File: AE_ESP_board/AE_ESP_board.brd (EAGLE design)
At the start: 72 x 49 mm, 26 parts, among them CN1 SW_UART_IF, CN2 HW_UART_IF, CN3 POWER_IF, Q1 2N7000, Q2 2N7000, SW1 10-XX, U1 AE-ESP-WROOM-02, U2 M78AR033-0.5

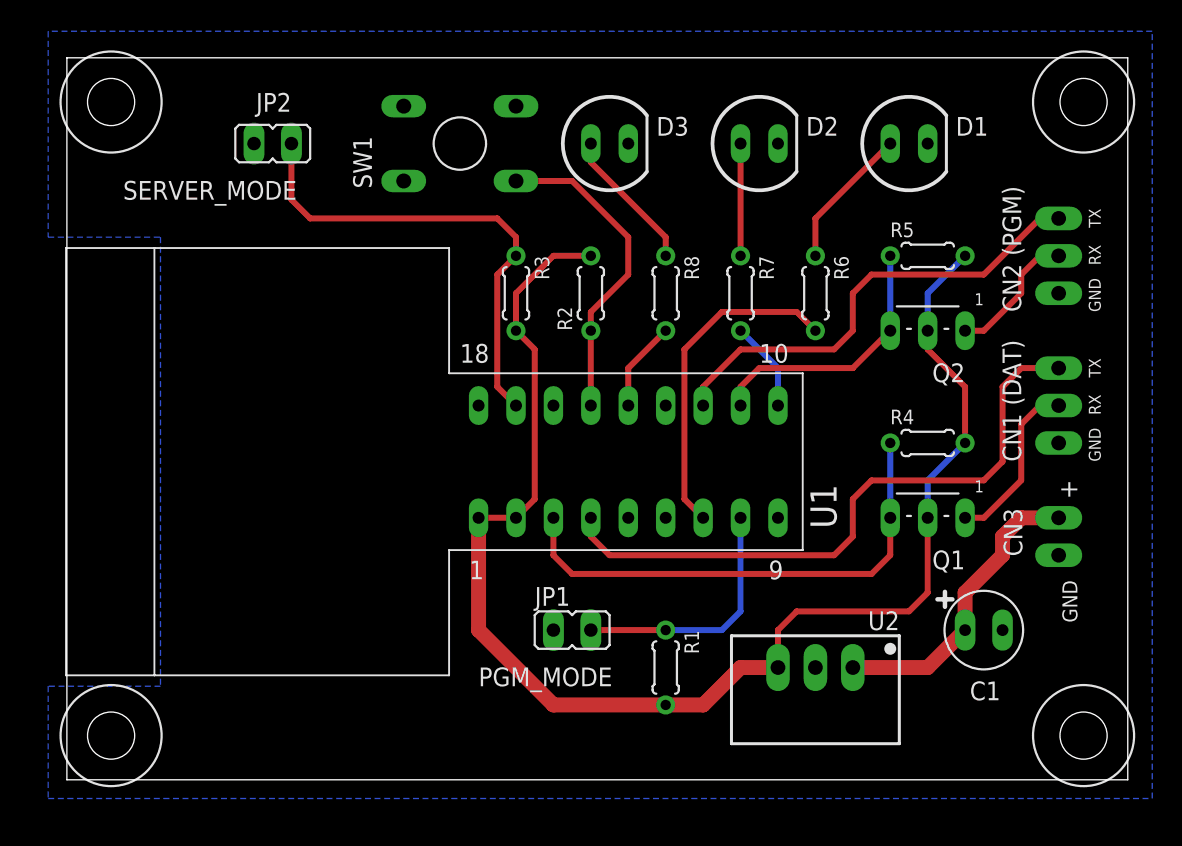
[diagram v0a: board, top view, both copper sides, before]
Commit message: レイアウトを修正
基板のサイズが間違っていたので修正
LEDのキャプションを追加
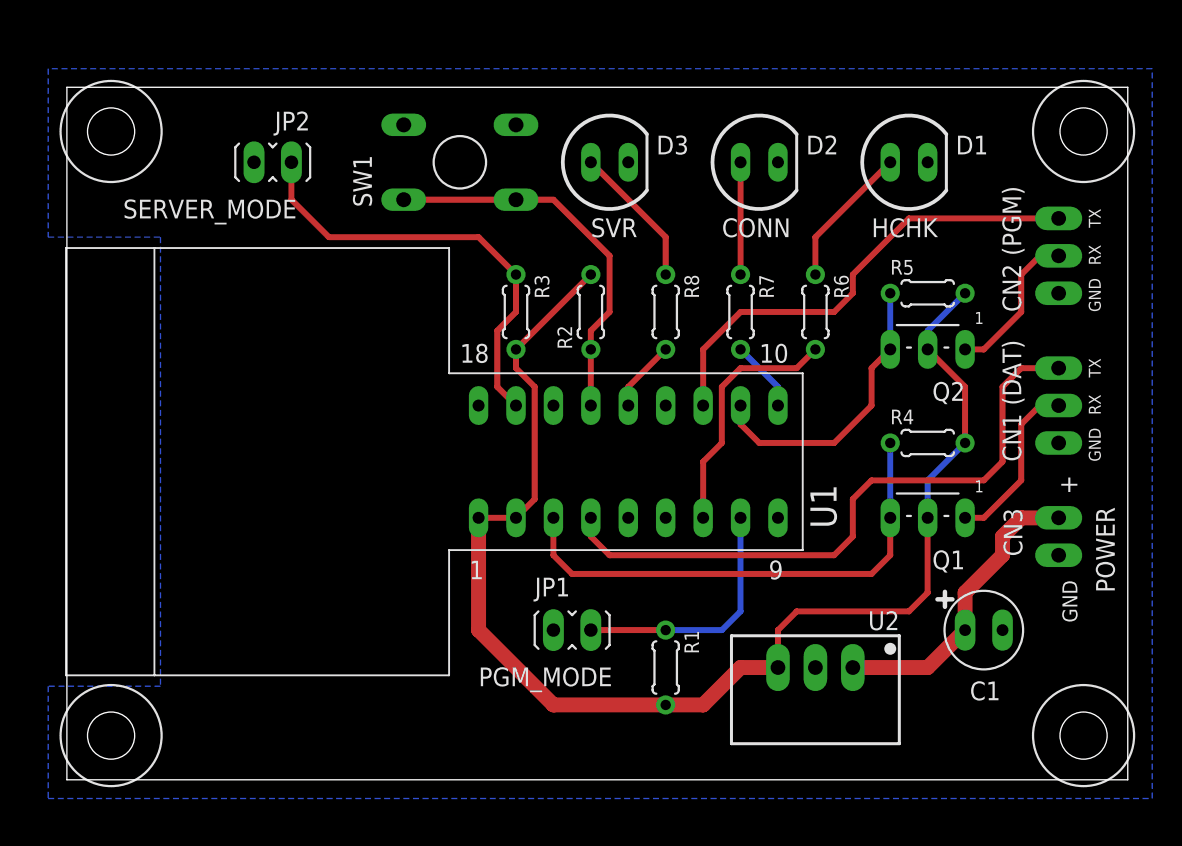
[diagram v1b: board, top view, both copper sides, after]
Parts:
- moved R5 2.54 mm to (58.4, 33.0)
- moved H1 2.00 mm to (69.0, 44.0)
- moved H2 2.00 mm to (3.00, 44.0)
- moved JP2 1.80 mm to (15.2, 41.9)
- moved D1 1.27 mm to (57.1, 41.9)
- moved D2 1.27 mm to (47.0, 41.9)
- moved D3 1.27 mm to (36.8, 41.9)
- moved R2 1.27 mm to (35.6, 31.8)
- moved R3 1.27 mm to (30.5, 31.8)
- moved R6 1.27 mm to (50.8, 31.8)
- moved R7 1.27 mm to (45.7, 31.8)
- moved R8 1.27 mm to (40.6, 31.8)
- moved SW1 1.27 mm to (22.9, 39.4)
- moved Q2 1.27 mm to (61.0, 29.2)
- moved JP1 1.27 mm to (33.0, 10.2)
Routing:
- net LED_HCHECK: track 22.4 -> 16.8 mm
- net +3V3: track 95.8 -> 90.5 mm
- net N$10: track 21.7 -> 26.2 mm
- net N$2: track 32.6 -> 29.8 mm
- net N$7: track 18.1 -> 19.9 mm
- net N$3: track 9.20 -> 10.5 mm
- net N$4: track 6.13 -> 4.86 mm
- net LED_CONNECTING: track 6.13 -> 4.86 mm
- net HW_UART_TXD: track 31.6 -> 32.4 mm
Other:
- board size 72 x 49 mm -> 72 x 47 mm
- board text added: "CONN"
- board text added: "HCHK"
- board text added: "POWER"
- board text added: "SVR"

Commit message: レイアウトの見直し
レイアウトを47mm x 47mm に縮小します。
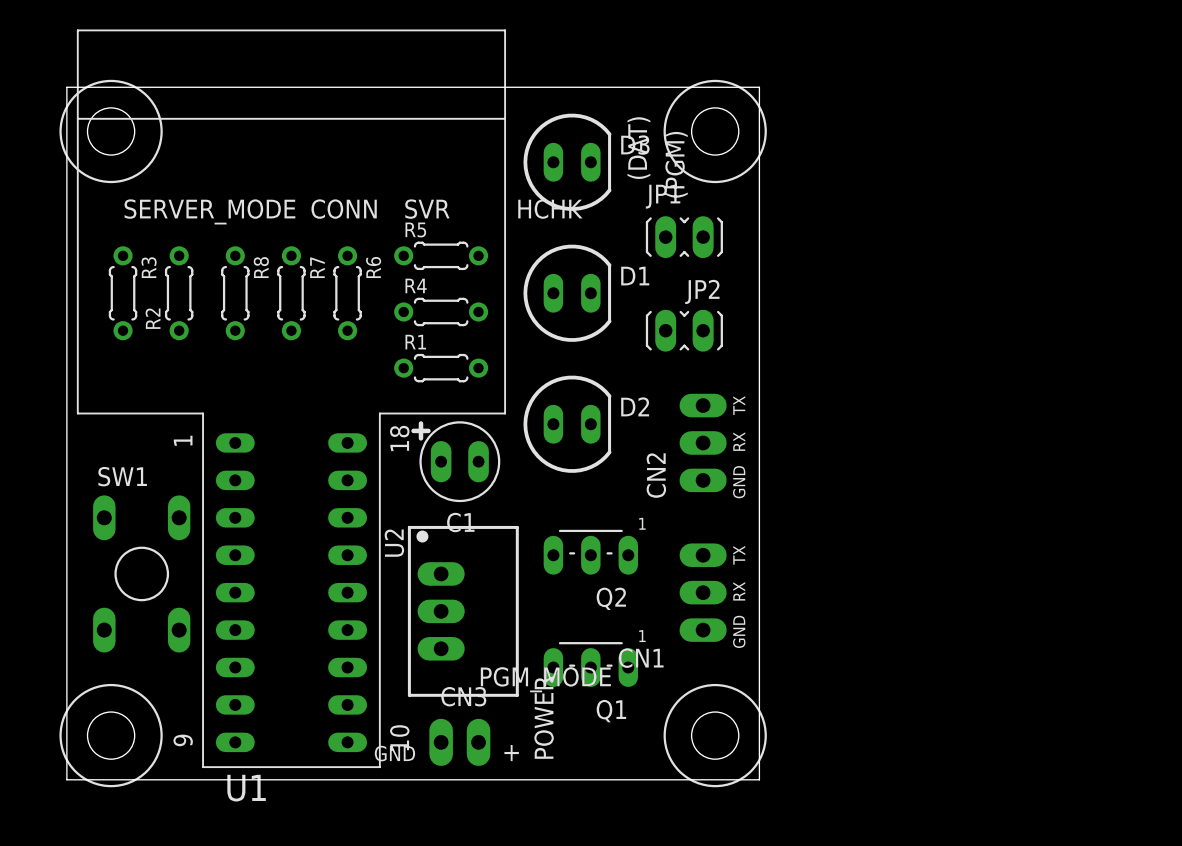
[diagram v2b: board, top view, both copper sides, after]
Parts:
- moved CN3 43.8 mm to (25.4, 2.54), turned to 0 degrees
- moved C1 37.4 mm to (26.7, 21.6)
- moved R4 34.2 mm to (25.4, 31.8)
- moved R5 33.1 mm to (25.4, 35.6)
- moved R6 31.8 mm to (19.1, 33.0)
- moved R7 30.5 mm to (15.2, 33.0)
- moved JP2 30.2 mm to (43.2, 30.5)
- moved SW1 29.6 mm to (2.54, 17.8), turned to 0 degrees
- moved R8 29.2 mm to (11.4, 33.0)
- moved U2 28.7 mm to (25.4, 14.0), turned to 270 degrees
- moved R2 28.0 mm to (7.62, 33.0)
- moved JP1 27.7 mm to (40.6, 36.8)
- moved CN2 27.3 mm to (43.2, 20.3)
- moved CN1 27.3 mm to (43.2, 10.2)
- moved Q2 26.8 mm to (38.1, 15.2)
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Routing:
- net +3V3: track 90.5 -> 0.00 mm
- net N$1: track 43.3 -> 0.00 mm
- net SW_UART_RXD_IN: track 34.1 -> 0.00 mm
- net HW_UART_TXD: track 32.4 -> 0.00 mm
- net N$2: track 29.8 -> 0.00 mm
- net N$10: track 26.2 -> 0.00 mm
- net +12V: track 20.4 -> 0.00 mm
- net N$7: track 19.9 -> 0.00 mm
- net N$9: track 17.0 -> 0.00 mm
- net LED_HCHECK: track 16.8 -> 0.00 mm
- net SW_UART_RXD: track 11.7 -> 0.00 mm
- net N$3: track 10.5 -> 0.00 mm
- net N$12: track 9.72 -> 0.00 mm
- net N$5: track 9.72 -> 0.00 mm
- net N$11: track 7.62 -> 0.00 mm
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- removed copper zone on layer 16, net 0V
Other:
- board size 72 x 47 mm -> 47 x 47 mm

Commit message: レイアウトを大幅見直し
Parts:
- D1, D2, D3: value LED_5MM -> LED_0805; device Parts:LED5MM -> Parts:CHIPLED_0805
- R6, R7, R8: device Parts:RESISTOR_0204_200MIL -> Parts:SMD_2012
- moved CN1 38.1 mm to (5.08, 8.89)
- moved SW1 36.9 mm to (39.4, 19.1)
- moved Q1 36.4 mm to (5.08, 22.9), turned to 270 degrees
- moved R8 21.6 mm to (31.1, 41.9), turned to 90 degrees
- moved R3 16.6 mm to (20.3, 34.3), turned to 180 degrees
- moved R4 16.5 mm to (10.2, 38.1)
- moved R7 16.3 mm to (31.1, 29.2), turned to 90 degrees
- moved CN2 16.1 mm to (38.1, 5.08), turned to 180 degrees
- moved R6 12.3 mm to (31.1, 35.6), turned to 90 degrees
- moved R1 11.4 mm to (20.3, 38.1)
- moved C1 7.73 mm to (34.3, 22.9)
- moved R5 7.18 mm to (20.3, 30.5), turned to 180 degrees
- moved Q2 5.39 mm to (34.3, 11.4), turned to 90 degrees
- moved D2 5.08 mm to (34.3, 29.2), turned to 90 degrees
- moved U2 5.08 mm to (25.4, 19.1)
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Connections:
- net 0V: now also D1.C, D2.C, D3.C; no longer D1.K, D2.K, D3.K
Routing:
- added copper zone on layer 16, net 0V
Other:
- board text added: "(DATA)"
- board text added: "(POWER)"
- board text added: "(PROG)"
- board text added: "CONNECT"
- board text added: "HCHECK"
- board text added: "SERVER"
- board text removed: "(DAT)"
- board text removed: "(PGM)"
- board text removed: "CONN"
- board text removed: "HCHK"
- board text removed: "POWER"
- board text removed: "SVR"

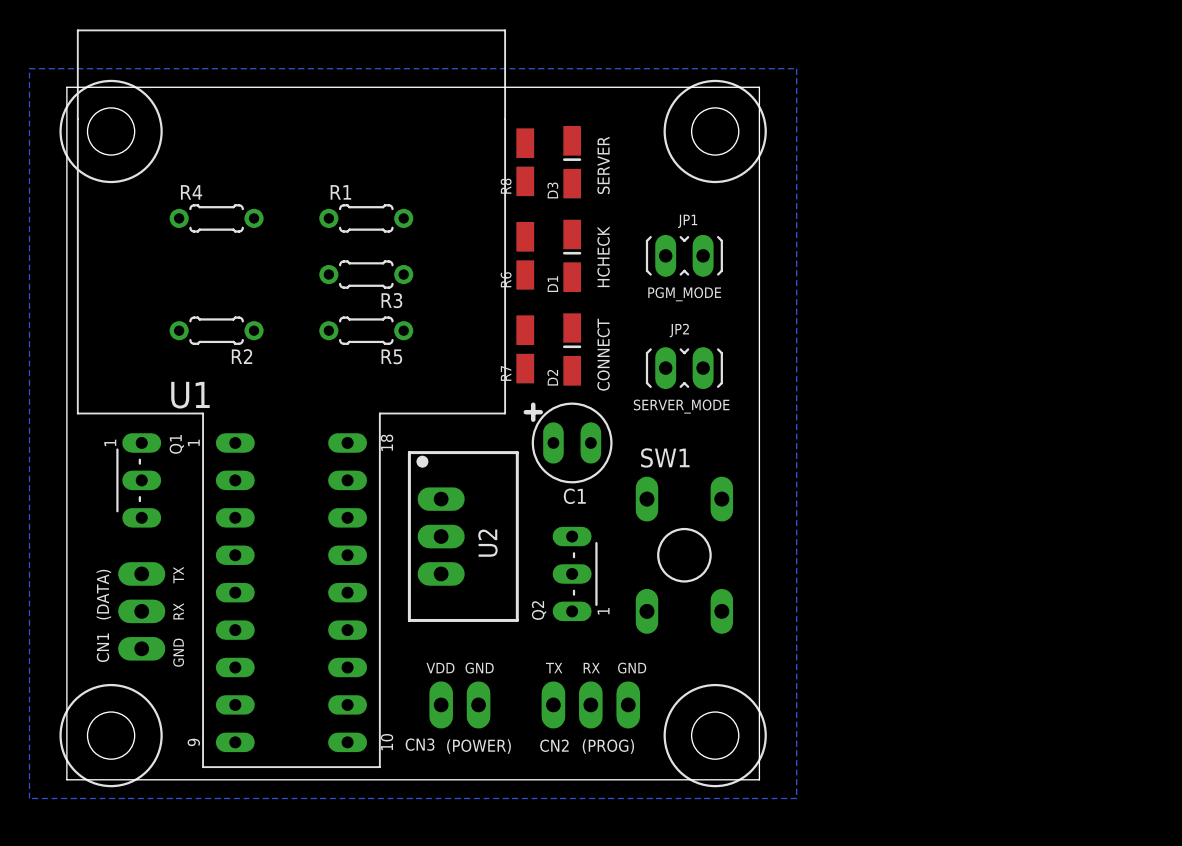
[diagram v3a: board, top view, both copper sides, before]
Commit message: レイアウト見直し
LED以外はリード部品とする
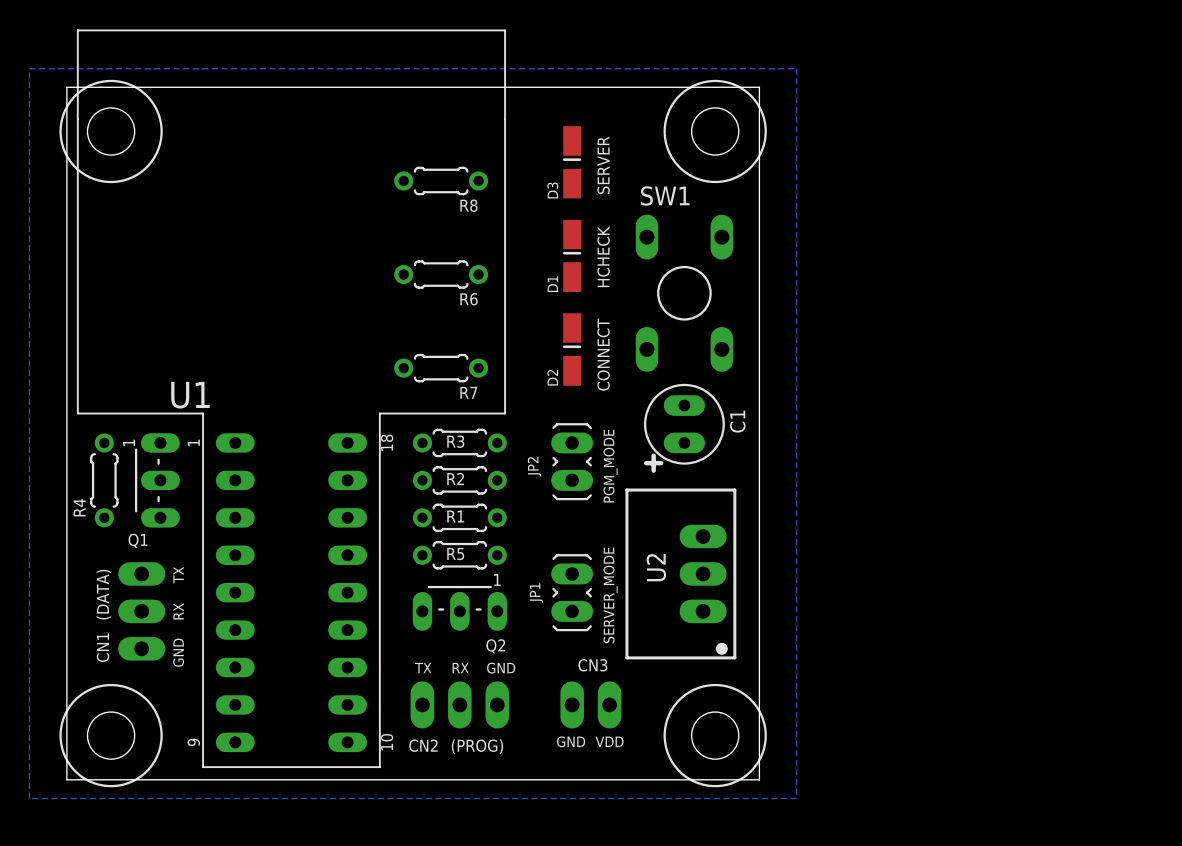
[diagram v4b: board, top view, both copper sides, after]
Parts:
- R6, R7, R8: device Parts:SMD_2012 -> Parts:RESISTOR_0204_200MIL
- moved JP1 23.3 mm to (34.3, 14.0), turned to 180 degrees
- moved R1 21.3 mm to (26.7, 17.8)
- moved R2 19.4 mm to (26.7, 20.3), turned to 0 degrees
- moved R4 19.3 mm to (2.54, 20.3), turned to 90 degrees
- moved U2 19.3 mm to (43.2, 11.4), turned to 90 degrees
- moved SW1 17.8 mm to (39.4, 36.8)
- moved R5 16.5 mm to (26.7, 15.2), turned to 0 degrees
- moved R3 13.1 mm to (26.7, 22.9), turned to 0 degrees
- moved JP2 9.92 mm to (34.3, 20.3), turned to 0 degrees
- moved CN2 8.89 mm to (29.2, 5.08)
- moved C1 7.73 mm to (41.9, 24.1), turned to 90 degrees
- moved CN3 6.35 mm to (34.3, 5.08), turned to 0 degrees
- moved R6 5.85 mm to (25.4, 34.3), turned to 180 degrees
- moved R7 5.85 mm to (25.4, 27.9), turned to 180 degrees
- moved R8 5.85 mm to (25.4, 40.6), turned to 180 degrees
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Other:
- board text removed: "(POWER)"
